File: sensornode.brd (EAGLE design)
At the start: 112.3 x 61 mm, 73 parts, among them IC1 CP2104, Q1 mmbt2222, Q2 mmbt2222, Q3 DMG3415U, SW2 KMR2, U1 TSL2591, U2 AP2112-3.3, U3 MCP73831T-2ACI/OT, U4 BMEx80, X2 ESP32_WROOM32_SKINNY, X4 20329

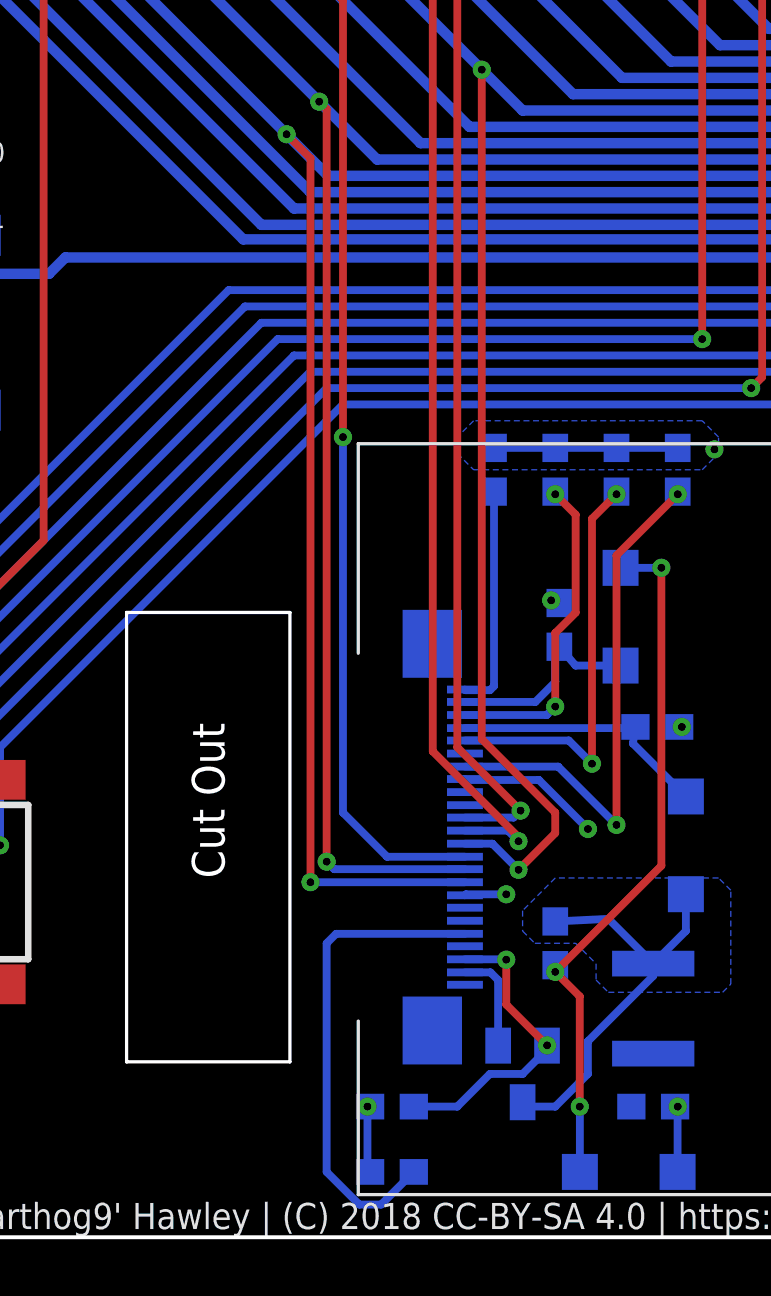
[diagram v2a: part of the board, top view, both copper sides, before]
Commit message: Moving traces around the FPC connector
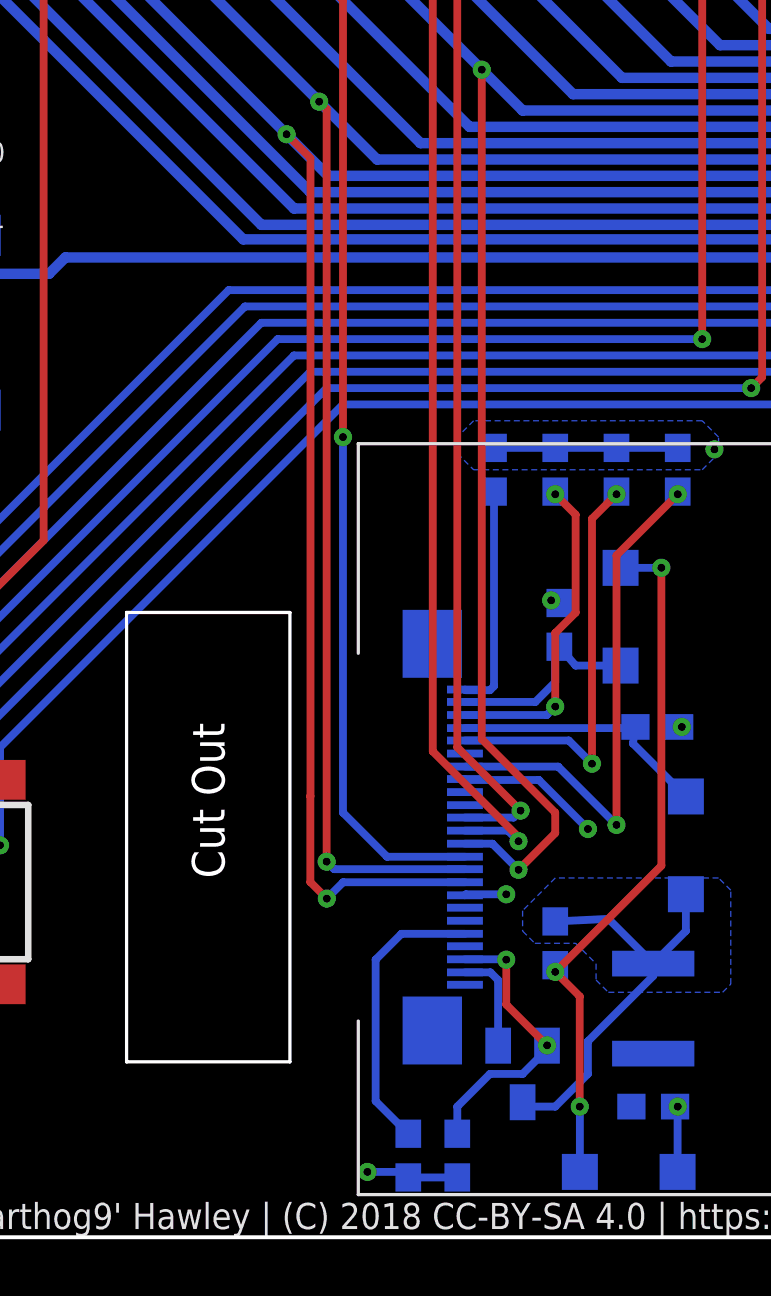
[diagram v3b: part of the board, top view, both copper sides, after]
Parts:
- moved R16 3.17 mm to (40.6, 3.17), turned to 270 degrees
- moved C14 0.90 mm to (38.7, 3.17), turned to 270 degrees
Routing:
- net N$20: track 18.9 -> 11.2 mm
- net GND: track 29.6 -> 30.5 mm
- net EINK_RESE: track 12.0 -> 11.4 mm
- net EINK_BUSY_A5_IO4: track 114.6 -> 115.1 mm
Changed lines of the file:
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@@
 </element>
 <element name="Q4" library="adafruit" package="SOT23" value="" x="43.18" y="6.35" rot="MR180"/>
-<element name="R16" library="SparkFun-Resistors" package="0603-RES" value="2.2" x="38.1" y="5.08" rot="MR0">
-<attribute name="PROD_ID" value="RES-07857" x="38.1" y="5.08" size="1.778" layer="28" rot="MR0" display="off"/>
+<element name="R16" library="SparkFun-Resistors" package="0603-RES" value="2.2" x="40.64" y="3.175" rot="MR270">
+<attribute name="PROD_ID" value="RES-07857" x="40.64" y="3.175" size="1.778" layer="28" rot="MR270" display="off"/>
 </element>
 <element name="U$15" library="Warthog9-Screens" package="WAVSHARE-BUYDISPLAY-2.13-THM" value="WAVSHARE-BUYDISPLAY-2.132.13-THROUGH" x="36.67125" y="22.5425" smashed="yes" rot="R180"/>
-<element name="C14" library="SparkFun-Capacitors" package="0603-CAP" value="1uF" x="38.1" y="2.54" rot="MR0">
-<attribute name="PROD_ID" value="CAP-08604" x="38.1" y="2.54" size="1.778" layer="28" rot="MR0" display="off"/>
+<element name="C14" library="SparkFun-Capacitors" package="0603-CAP" value="1uF" x="38.735" y="3.175" rot="MR270">
+<attribute name="PROD_ID" value="CAP-08604" x="38.735" y="3.175" size="1.778" layer="28" rot="MR270" display="off"/>
 </element>
 <element name="C15" library="SparkFun-Capacitors" package="0603-CAP" value="1uF" x="49.2125" y="29.845" rot="MR90">
@@
 <wire x1="49.2075" y1="2.54" x2="49.2075" y2="5.075" width="0.3048" layer="16"/>
 <wire x1="49.2075" y1="5.075" x2="49.2125" y2="5.08" width="0.3048" layer="16"/>
-<wire x1="37.25" y1="5.08" x2="37.1475" y2="5.08" width="0.3048" layer="16"/>
-<via x="37.1475" y="5.08" extent="1-16" drill="0.3048"/>
-<wire x1="37.1475" y1="5.08" x2="37.1475" y2="2.6425" width="0.3048" layer="16"/>
-<wire x1="37.1475" y1="2.6425" x2="37.25" y2="2.54" width="0.3048" layer="16"/>
+<via x="37.1475" y="2.54" extent="1-16" drill="0.3048"/>
 <wire x1="40.93845" y1="17.8181" x2="40.90035" y2="17.78" width="0.3048" layer="16"/>
 <wire x1="42.38625" y1="31.0125" x2="42.06875" y2="30.695" width="0.3048" layer="16"/>
@@
 <vertex x="40.64" y="30.48"/>
 </polygon>
+<wire x1="40.64" y1="2.325" x2="38.735" y2="2.325" width="0.3048" layer="16"/>
+<wire x1="38.735" y1="2.325" x2="38.52" y2="2.54" width="0.3048" layer="16"/>
+<wire x1="38.52" y1="2.54" x2="37.1475" y2="2.54" width="0.3048" layer="16"/>
 <wire x1="96.995" y1="44.4275" x2="94.615" y2="43.18" width="0" layer="19" extent="1-1"/>
 </signal>
@@
 <wire x1="19.475" y1="57.41625" x2="34.000625" y2="42.890625" width="0.4064" layer="16"/>
 <wire x1="34.000625" y1="42.890625" x2="35.61625" y2="41.275" width="0.4064" layer="16"/>
-<wire x1="40.93845" y1="13.8049" x2="34.93135" y2="13.8049" width="0.3048" layer="16"/>
-<via x="34.93135" y="13.8049" extent="1-16" drill="0.3048"/>
-<wire x1="34.93135" y1="13.8049" x2="34.93135" y2="41.9599" width="0.3048" layer="1"/>
+<via x="35.56635" y="13.1699" extent="1-16" drill="0.3048"/>
 <wire x1="34.93135" y1="41.9599" x2="34.000625" y2="42.890625" width="0.3048" layer="1"/>
 <via x="34.000625" y="42.890625" extent="1-16" drill="0.3048"/>
+<wire x1="40.93845" y1="13.8049" x2="36.20135" y2="13.8049" width="0.3048" layer="16"/>
+<wire x1="36.20135" y1="13.8049" x2="35.56635" y2="13.1699" width="0.3048" layer="16"/>
+<wire x1="35.56635" y1="13.1699" x2="34.925" y2="13.81125" width="0.3048" layer="1"/>
+<wire x1="34.925" y1="13.81125" x2="34.925" y2="17.145" width="0.3048" layer="1"/>
+<wire x1="34.925" y1="17.145" x2="34.93135" y2="17.15135" width="0.3048" layer="1"/>
+<wire x1="34.93135" y1="17.15135" x2="34.93135" y2="41.9599" width="0.3048" layer="1"/>
 </signal>
 <signal name="EINK_MOSI_IO23">
@@
 <wire x1="43.18" y1="6.35" x2="41.91" y2="6.35" width="0.3048" layer="16"/>
 <wire x1="41.91" y1="6.35" x2="40.64" y2="5.08" width="0.3048" layer="16"/>
-<wire x1="40.64" y1="5.08" x2="38.95" y2="5.08" width="0.3048" layer="16"/>
+<wire x1="40.64" y1="5.08" x2="40.64" y2="4.025" width="0.3048" layer="16"/>
 <wire x1="44.13" y1="7.45" x2="44.13" y2="7.45875" width="0.3048" layer="16"/>
 <wire x1="44.13" y1="7.45875" x2="44.1325" y2="7.46125" width="0.3048" layer="16"/>
@@
 <contactref element="U$15" pad="5-VGH"/>
 <contactref element="C14" pad="1"/>
-<wire x1="40.93845" y1="11.7983" x2="35.9283" y2="11.7983" width="0.3048" layer="16"/>
-<wire x1="35.9283" y1="11.7983" x2="35.56" y2="11.43" width="0.3048" layer="16"/>
-<wire x1="35.56" y1="11.43" x2="35.56" y2="2.54" width="0.3048" layer="16"/>
-<wire x1="35.56" y1="2.54" x2="36.83" y2="1.27" width="0.3048" layer="16"/>
-<wire x1="36.83" y1="1.27" x2="37.68" y2="1.27" width="0.3048" layer="16"/>
-<wire x1="37.68" y1="1.27" x2="38.95" y2="2.54" width="0.3048" layer="16"/>
+<wire x1="40.93845" y1="11.7983" x2="38.4683" y2="11.7983" width="0.3048" layer="16"/>
+<wire x1="38.4683" y1="11.7983" x2="37.465" y2="10.795" width="0.3048" layer="16"/>
+<wire x1="37.465" y1="10.795" x2="37.465" y2="5.295" width="0.3048" layer="16"/>
+<wire x1="37.465" y1="5.295" x2="38.735" y2="4.025" width="0.3048" layer="16"/>
 </signal>
 <signal name="N$16">

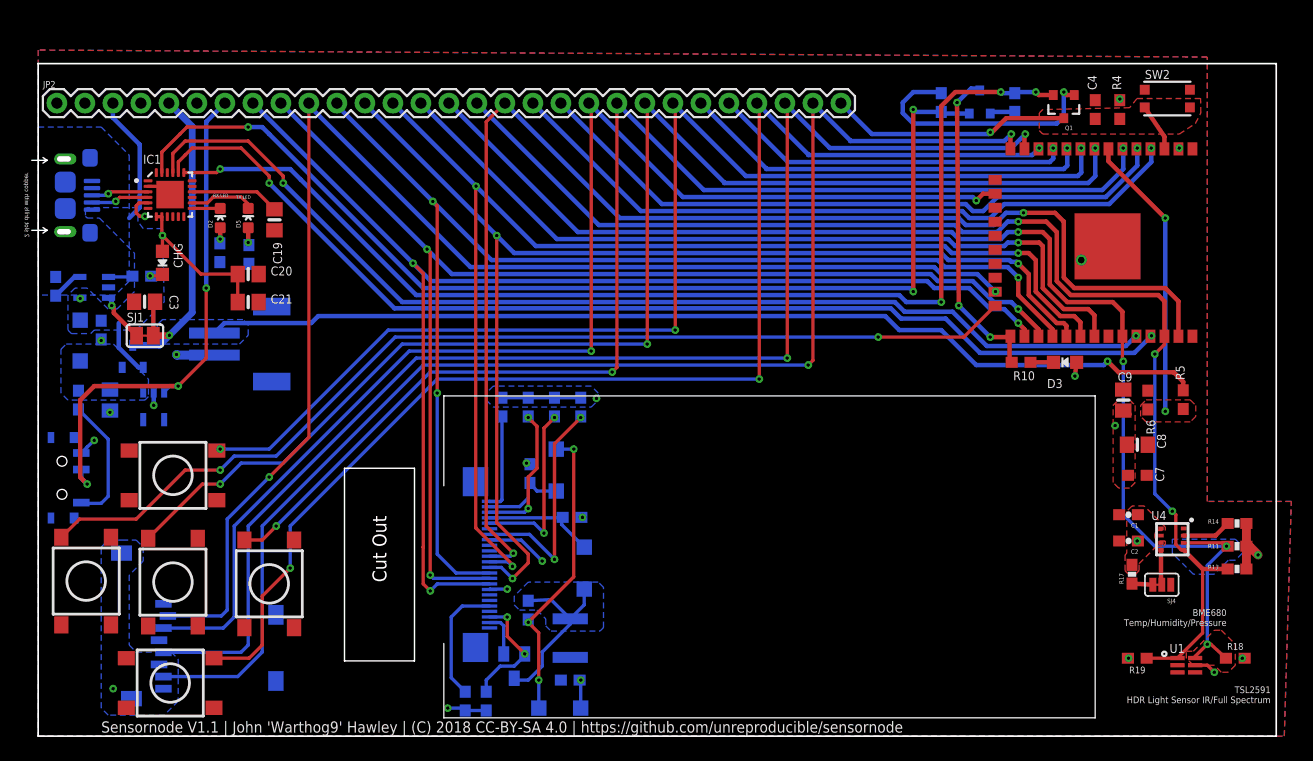
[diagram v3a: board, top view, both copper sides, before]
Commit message: Updating the FPC + part for the e-ink screen
Think I had the pinout on the FPC backwards.  This should flip it
and move a bunch of pieces around as a result
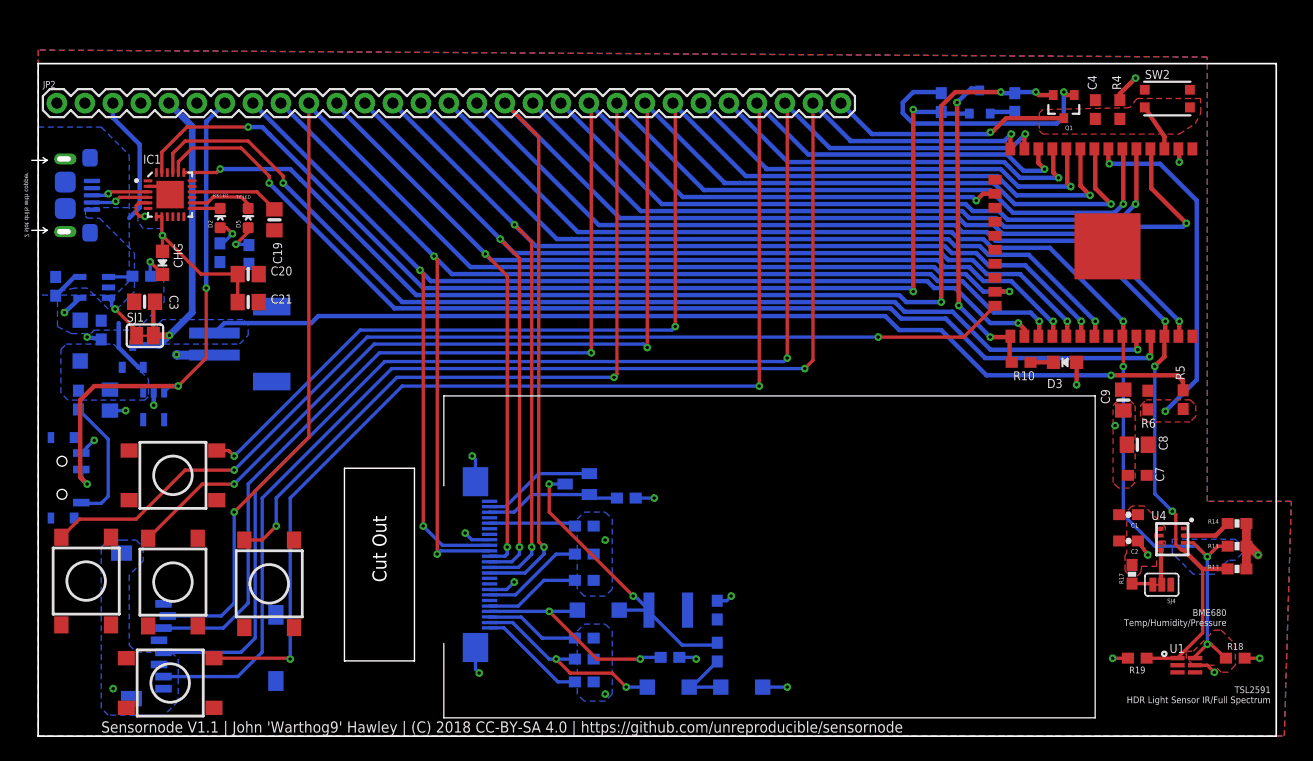
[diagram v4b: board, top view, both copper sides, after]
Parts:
- moved C18 26.0 mm to (49.5, 4.92), turned to 180 degrees
- moved R16 22.4 mm to (53.3, 21.6), turned to 180 degrees
- moved D1 22.2 mm to (57.1, 4.45), turned to 0 degrees
- moved C17 21.6 mm to (49.5, 8.89), turned to 180 degrees
- moved C14 19.2 mm to (49.5, 19.1), turned to 180 degrees
- moved C12 17.6 mm to (61.6, 7.62)
- moved C11 17.5 mm to (49.5, 6.99), turned to 0 degrees
- moved Q4 17.5 mm to (48.9, 22.9), turned to 270 degrees
- moved D6 16.6 mm to (63.8, 4.45)
- moved C16 15.9 mm to (49.5, 14.1), turned to 180 degrees
- moved C10 15.5 mm to (57.3, 7.14)
- moved C13 14.8 mm to (61.6, 11.4), turned to 90 degrees
- moved C15 13.3 mm to (49.5, 16.5), turned to 180 degrees
- moved L1 9.25 mm to (57.1, 11.4), turned to 180 degrees
- moved D7 4.02 mm to (50.8, 11.4), turned to 180 degrees
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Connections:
- net EINK_MOSI_IO23: now also U$15.14-DI; no longer U$15.14-D1
- net EINK_SCLK_MOSI: now also U$15.13-DO; no longer U$15.13-D0
- net GND: now also U$15.25, U$15.26
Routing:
- net N$11: track 27.5 -> 6.38 mm, vias 3 -> 0
- net N$16: track 20.8 -> 9.27 mm, vias 2 -> 0
- net N$14: track 16.2 -> 27.1 mm, vias 0 -> 2
- net EINK_VGL: track 7.97 -> 18.4 mm, vias 0 -> 2
- net EINK_VGH: track 10.2 -> 20.0 mm, vias 0 -> 2
- net 3.3V: track 12.7 -> 22.3 mm
- net A4_IO36: track 63.9 -> 72.3 mm
- net EINK_DC_IO17: track 112.8 -> 104.5 mm
- net N$17: track 16.3 -> 8.71 mm, vias 2 -> 0
- net BTN-IO27_A10: track 117.9 -> 124.8 mm
- net EINK_GDR: track 3.96 -> 10.3 mm
- net EINK_BUSY_A5_IO4: track 115.1 -> 109.2 mm
- net BTN-IO32_A7: track 121.3 -> 126.8 mm
- net BTN-A2_I34: track 116.2 -> 121.6 mm
- net SDA: track 118.8 -> 113.4 mm
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- removed copper zone on layer 16, net N$14

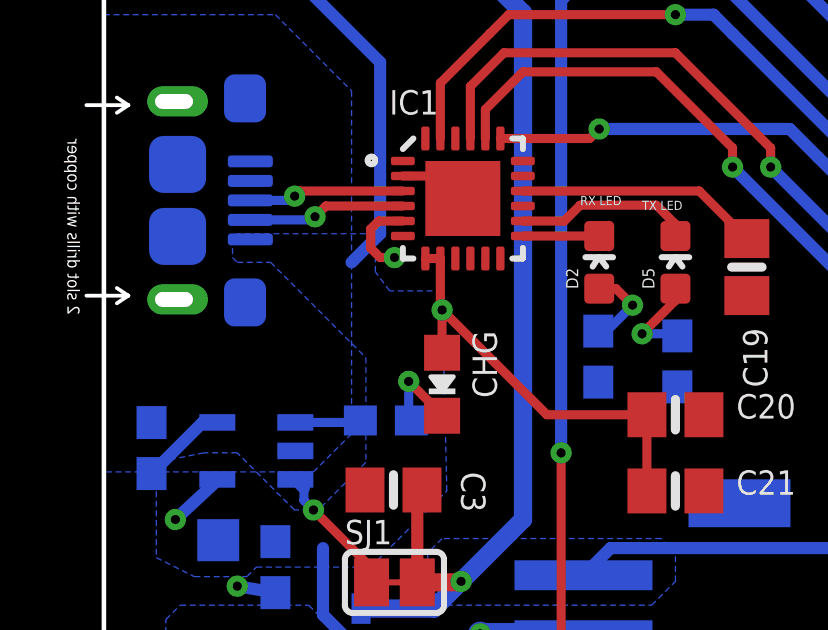
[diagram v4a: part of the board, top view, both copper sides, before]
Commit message: Adding a 10uF Cap to the CP2104
This make it more closely resemble the known working designs.
Getting paranoid due to when this will need to get built.
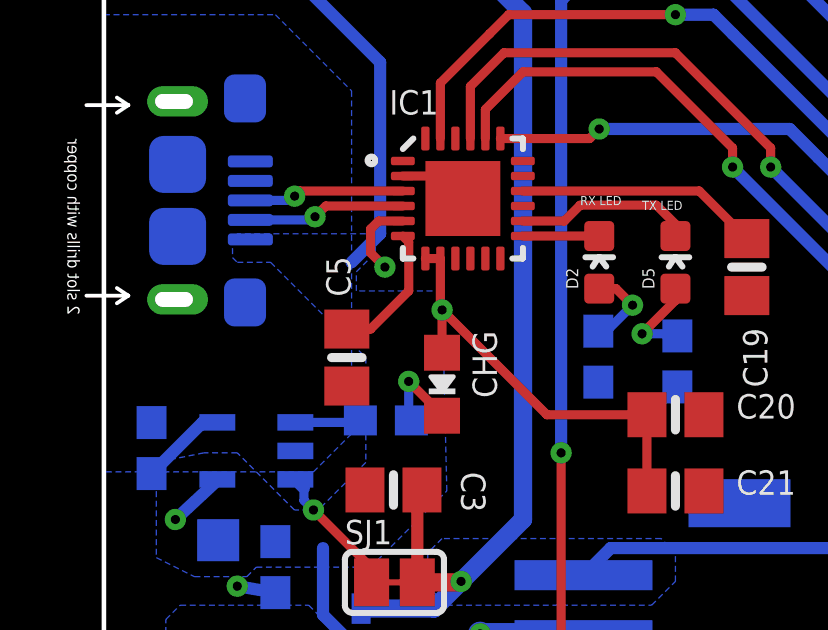
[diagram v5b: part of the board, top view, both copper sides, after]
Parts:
- added C5: 10uF, microbuilder:0805-NO
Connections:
- removed net VDD: IC1.6
- new net N$6: C5.2, IC1.6
- net GND: now also C5.1
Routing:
- net N$6: track 0.00 -> 4.50 mm
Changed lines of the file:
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@@
 <element name="C21" library="microbuilder" package="0805-NO" value="0.1uF" x="19.05" y="39.37"/>
 <element name="U$17" library="adafruit" package="MICROSD" value="MICROSD" x="22" y="3" rot="MR90"/>
+<element name="C5" library="microbuilder" package="0805-NO" value="10uF" x="8.09625" y="43.815" rot="R90"/>
 </elements>
 <signals>
@@
 <wire x1="97.17625" y1="44.60875" x2="96.995" y2="44.4275" width="0.8128" layer="1"/>
 <wire x1="39.66845" y1="25.10155" x2="39.37" y2="25.4" width="0.3048" layer="16"/>
+<contactref element="C5" pad="1"/>
 </signal>
 <signal name="TXLED">
@@
 <vertex x="11.43" y="39.37"/>
 <vertex x="11.27125" y="46.0375"/>
-<vertex x="9.525" y="46.0375"/>
-<vertex x="9.04875" y="46.6725"/>
+<vertex x="8.41375" y="46.0375"/>
+<vertex x="8.41375" y="46.6725"/>
+<vertex x="9.04875" y="47.3075"/>
 <vertex x="9.04875" y="47.9425"/>
 <vertex x="4.445" y="47.9425"/>
@@
 <wire x1="9.96484375" y1="48.367246875" x2="9.155996875" y2="48.367246875" width="0.3048" layer="1"/>
 <wire x1="9.155996875" y1="48.367246875" x2="8.89" y2="48.10125" width="0.3048" layer="1"/>
-<wire x1="8.89" y1="48.10125" x2="8.89" y2="47.46625" width="0.3048" layer="1"/>
-<wire x1="8.89" y1="47.46625" x2="9.2075" y2="47.14875" width="0.3048" layer="1"/>
-<wire x1="9.2075" y1="47.14875" x2="9.68375" y2="47.14875" width="0.3048" layer="1"/>
-<via x="9.68375" y="47.14875" extent="1-16" drill="0.3048"/>
+<via x="9.36625" y="46.83125" extent="1-16" drill="0.3048"/>
 <polygon width="0.3048" layer="1">
 <vertex x="98.5" y="30.5"/>
@@
 <wire x1="98.1075" y1="57.6825" x2="98.1075" y2="58.26125" width="0.4064" layer="1"/>
 <wire x1="98.1075" y1="58.26125" x2="99.53625" y2="59.69" width="0.4064" layer="1"/>
+<wire x1="8.89" y1="48.10125" x2="8.89" y2="47.3075" width="0.3048" layer="1"/>
+<wire x1="8.89" y1="47.3075" x2="9.36625" y2="46.83125" width="0.3048" layer="1"/>
 </signal>
 <signal name="RESET">
@@
 <wire x1="47.14875" y1="4.92125" x2="48.68" y2="4.92125" width="0.3048" layer="16"/>
 </signal>
-<signal name="VDD">
-<contactref element="IC1" pad="6"/>
-</signal>
 <signal name="N$23">
 <contactref element="C19" pad="1"/>
@@
 <wire x1="19.845253125" y1="49.367246875" x2="21.43125" y2="47.78125" width="0.3048" layer="1"/>
 </signal>
+<signal name="N$6">
+<contactref element="IC1" pad="6"/>
+<contactref element="C5" pad="2"/>
+<wire x1="10.16" y1="46.0375" x2="8.8875" y2="44.765" width="0.3048" layer="1"/>
+<wire x1="8.8875" y1="44.765" x2="8.09625" y2="44.765" width="0.3048" layer="1"/>
+<wire x1="10.16" y1="46.0375" x2="10.16" y2="47.672090625" width="0.3048" layer="1"/>
+<wire x1="10.16" y1="47.672090625" x2="9.96484375" y2="47.867246875" width="0.3048" layer="1"/>
+</signal>
 </signals>
